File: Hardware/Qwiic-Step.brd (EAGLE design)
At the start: 50.8 x 50.8 mm, 99 parts, among them J1 PTH, J2 Qwiic Right Angle, J3 5.5x2.1mm Barrel, J4 Qwiic Right Angle, J5 ISP, U1 A4988ALT1, U2 ATMEGA328P_TQFP, Y1 16MHz

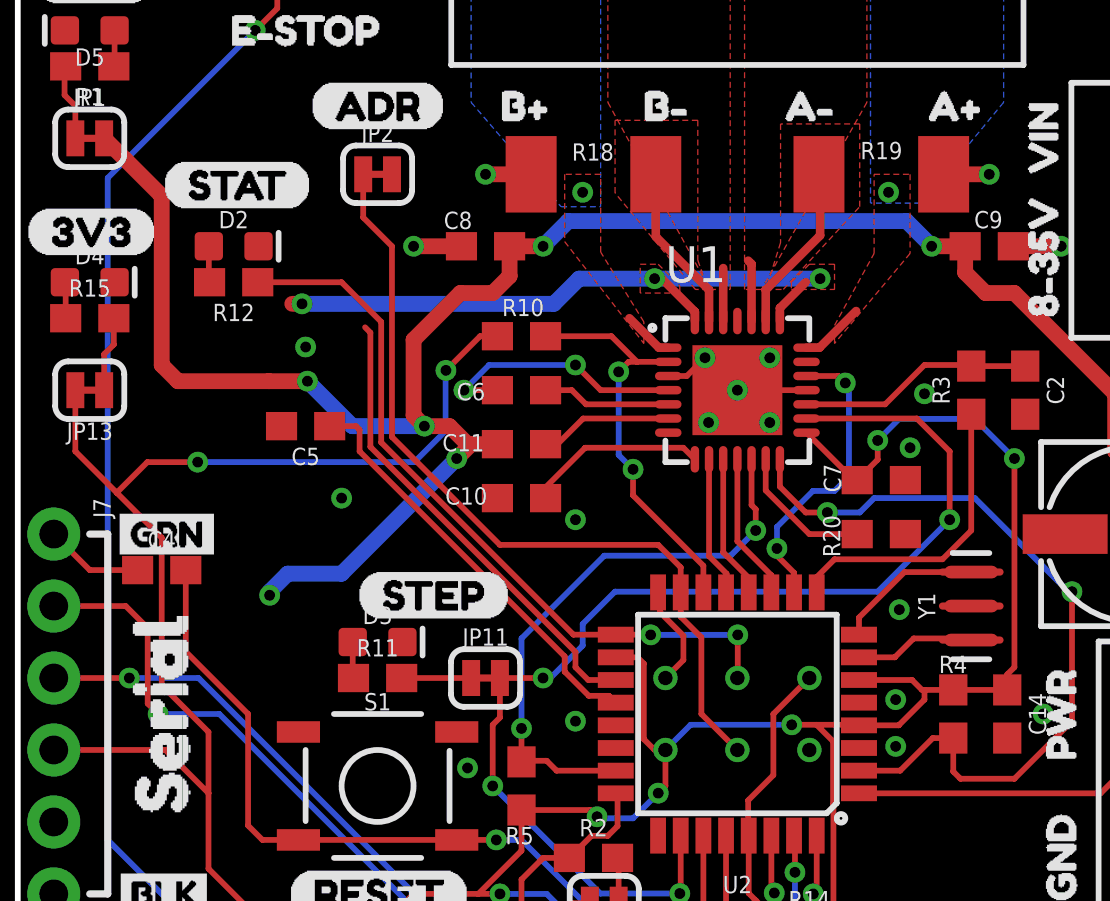
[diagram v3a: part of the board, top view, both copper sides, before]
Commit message: Cleaning up Rev 1 changes. Still need to connect current sense trace, run DRC.
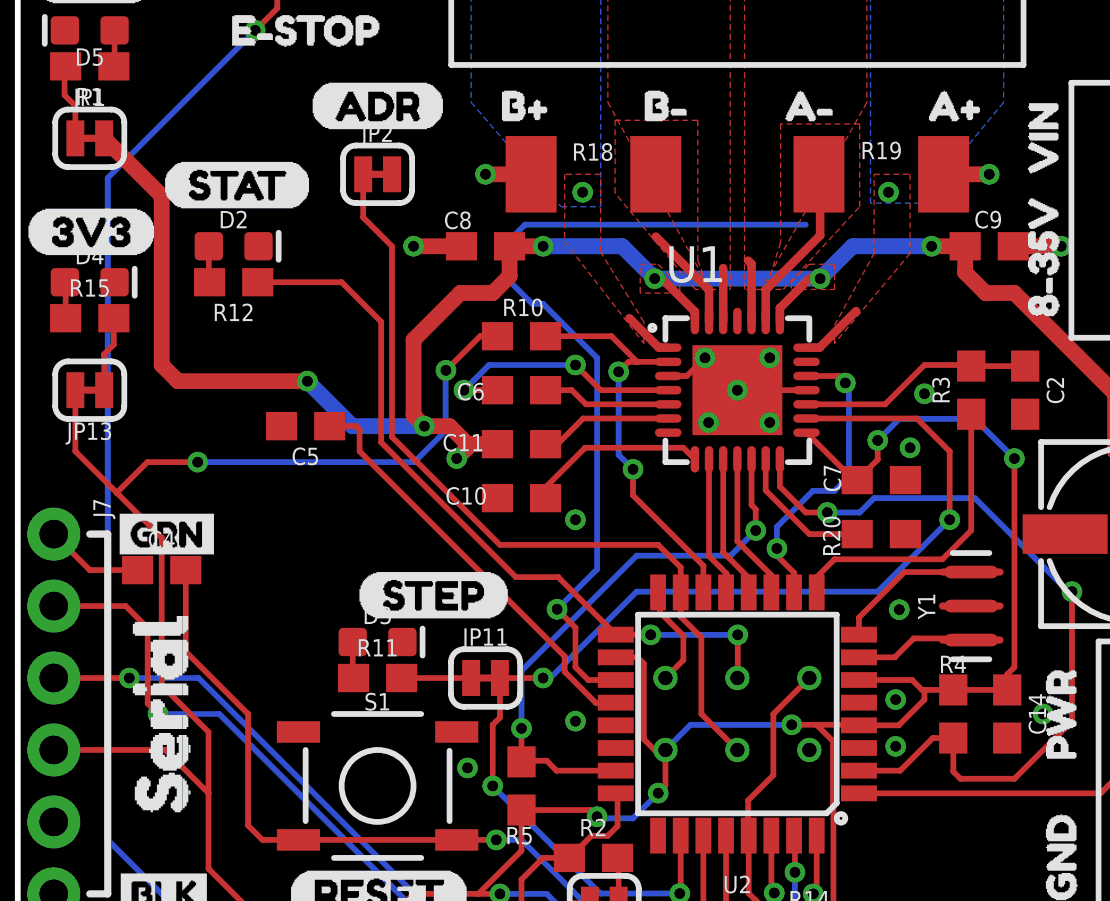
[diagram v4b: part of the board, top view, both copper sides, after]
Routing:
- net VIN: track 101.7 -> 74.8 mm, vias 9 -> 7
- net CURRENT_SENSE: track 22.7 -> 35.6 mm, vias 0 -> 1
- net N$31: track 5.96 -> 3.76 mm
- net A49885_!RESET!: track 20.2 -> 19.6 mm
- net GND: vias 22 -> 20

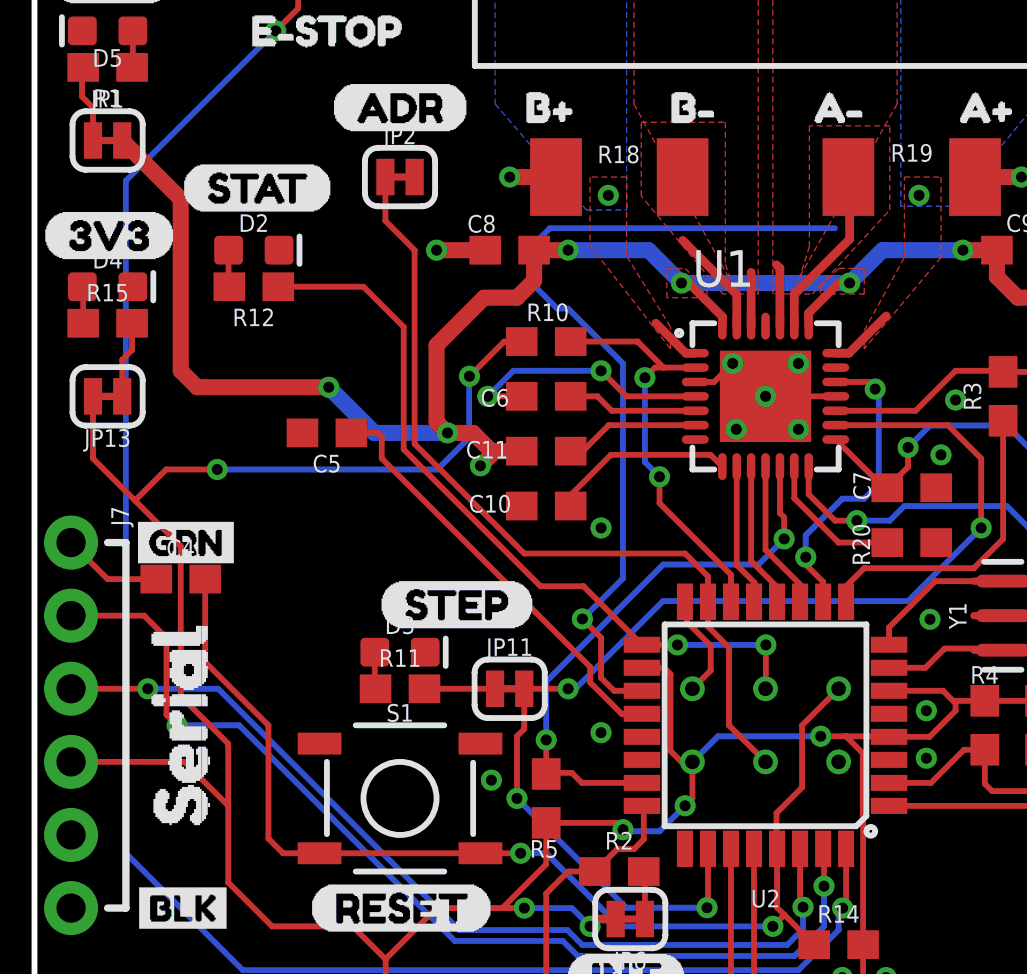
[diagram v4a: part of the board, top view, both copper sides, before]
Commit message: Added amplifier circuit to current sense reading
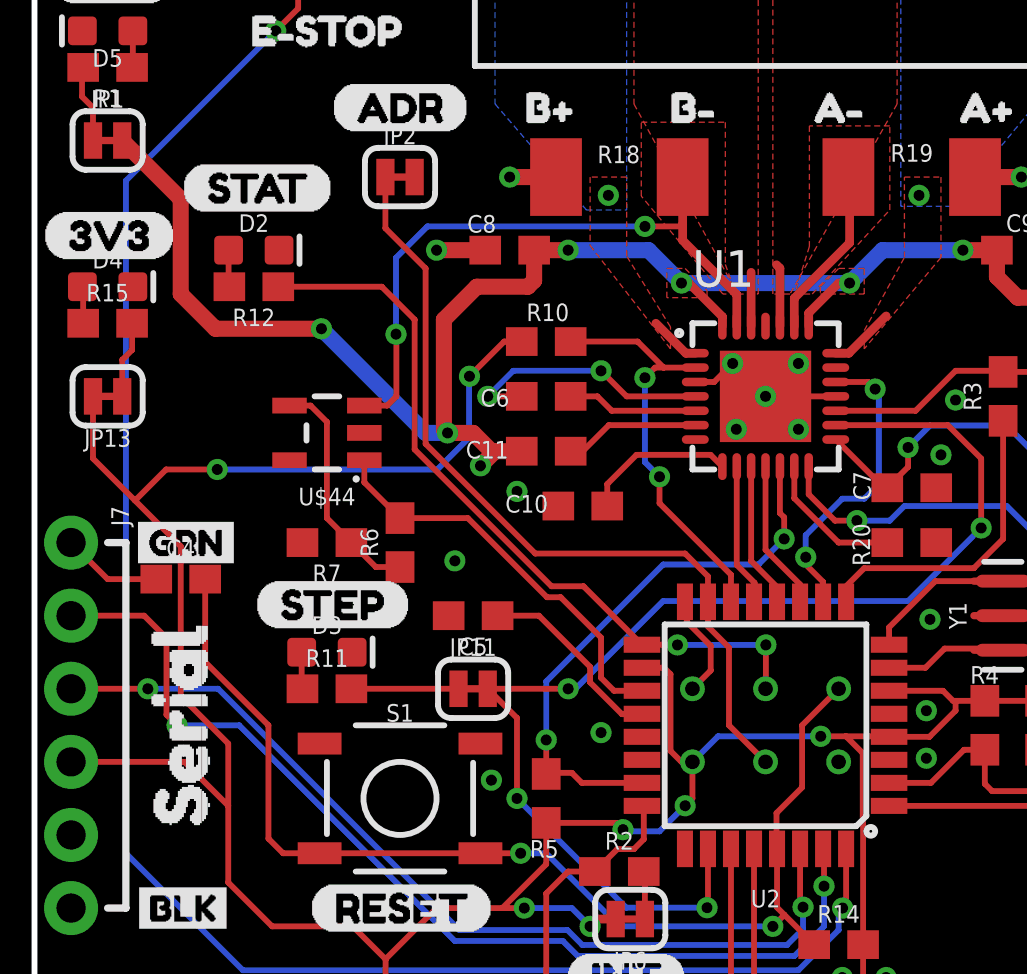
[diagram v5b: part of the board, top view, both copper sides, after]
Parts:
- added R6: 300k, SparkFun-Resistors:0603
- added R7: 1k, SparkFun-Resistors:0603
- added U$44: OPA344, SparkFun-IC-Amplifiers:SOT23-5
- moved C5 8.13 mm to (15.2, 19.1)
- moved U$32 7.62 mm to (36.8, 35.6)
- moved U$19 7.62 mm to (27.4, 31.5)
- moved LOGO1 7.49 mm to (20.2, 31.5)
- moved U$36 5.08 mm to (34.8, 41.8)
- moved U$37 5.08 mm to (29.7, 41.8)
- moved U$38 5.08 mm to (19.6, 41.8)
- moved U$39 5.08 mm to (24.5, 41.8)
- moved U$7 4.32 mm to (7.62, 19.4)
- moved D3 2.54 mm to (10.2, 17.8)
- moved R11 2.54 mm to (10.2, 16.5)
- moved JP11 1.27 mm to (15.2, 16.5)
- moved C10 1.27 mm to (19.1, 22.9)
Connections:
- removed net N$31: R18.2, U1.27
- new net AMP_CUR_SENSE: R6.2, U$44.1, U2.19
- new net N$2: R6.1, R7.1, U$44.4
- new net N$3: R19.2, U1.23
- net CURRENT_SENSE: now also R18.2, U$44.3, U1.27; no longer R19.2, U1.23, U2.19
- net GND: now also R7.2
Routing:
- net AMP_CUR_SENSE: track 0.00 -> 14.3 mm
- net CURRENT_SENSE: track 35.6 -> 22.5 mm, vias 1 -> 2
- net AREF: track 14.9 -> 6.76 mm
- net N$2: track 0.00 -> 8.12 mm
- net N$3: track 0.00 -> 5.99 mm
- net N$31: track 3.76 -> 0.00 mm
- net STEP: track 40.3 -> 41.9 mm
- net VIN: track 74.8 -> 73.4 mm
- net N$11: track 2.45 -> 3.72 mm
- net N$20: track 6.40 -> 5.35 mm
- net GND: vias 20 -> 21
- removed copper zone on layer 1, net N$31

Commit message: All traces routed, READY FOR BOARD REVIEW (other than some minor silk updates that I'll do tomorrow morning).
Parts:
- removed R6: 300k, SparkFun-Resistors:0603
- removed U$39: (no value), buzzard_labels (15):B#3
- added R9: 22k, SparkFun-Resistors:0603
- added U$45: (no value), buzzard_labels (28):3V31
- added U$46: (no value), buzzard_labels (28):A#3
- added U$47: (no value), buzzard_labels (28):A#4
- added U$48: (no value), buzzard_labels (28):B#5
- added U$49: (no value), buzzard_labels (28):B#6
- U$15: device buzzard_labels (15):A#0 -> buzzard_labels (28):A#3
- U$16: device buzzard_labels (15):A#1 -> buzzard_labels (28):A#4
- U$17: device buzzard_labels (15):B#2 -> buzzard_labels (28):B#5
- U$18: device buzzard_labels (15):B#3 -> buzzard_labels (28):B#6
- U$36: device buzzard_labels (15):A#0 -> buzzard_labels (28):PWR7
- U$37: device buzzard_labels (15):A#1 -> buzzard_labels (28):STEP2
- U$38: device buzzard_labels (15):B#2 -> buzzard_labels (28):VIN0
- moved U$36 29.9 mm to (41.9, 12.7), turned to 90 degrees
- moved U$37 23.7 mm to (8.89, 30.5)
- moved U$25 22.6 mm to (20.2, 16.4), flipped to the bottom
- moved JP2 20.9 mm to (17.8, 14.0), flipped to the bottom
- moved JP11 14.5 mm to (11.4, 30.5), flipped to the bottom
- moved R11 14.0 mm to (11.4, 30.5)
- moved U$7 13.3 mm to (0.25, 30.5)
- moved D3 13.0 mm to (7.62, 30.5), turned to 180 degrees
- moved JP13 12.6 mm to (11.4, 35.6), flipped to the bottom, turned to 0 degrees
- moved U$38 11.3 mm to (8.89, 38.1)
- moved R15 10.9 mm to (11.4, 35.6)
- moved R7 10.2 mm to (15.2, 30.5), turned to 90 degrees
- moved U$44 10.2 mm to (19.1, 30.5)
- moved JP1 9.25 mm to (11.4, 38.1), flipped to the bottom
- moved R1 8.89 mm to (11.4, 38.1), turned to 0 degrees
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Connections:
- new net N$6: JP2.1, U2.22
- net AMP_CUR_SENSE: now also R9.2; no longer R6.2
- net MOSI: no longer JP2.1
- net N$2: now also R9.1; no longer R6.1
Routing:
- net MOSI: track 28.8 -> 6.39 mm
- net STEP: track 41.9 -> 63.4 mm
- net CURRENT_SENSE: track 22.5 -> 8.49 mm, vias 2 -> 0
- net N$21: track 4.71 -> 14.3 mm
- net N$20: track 5.35 -> 13.2 mm
- net N$9: track 4.54 -> 11.0 mm
- net 3.3V: track 153.7 -> 147.3 mm
- net !ENABLE!: track 14.5 -> 20.2 mm
- net AMP_CUR_SENSE: track 14.3 -> 19.9 mm, vias 0 -> 2
- net COILB+: track 1.80 -> 6.92 mm, vias 1 -> 2
- net N$8: track 9.13 -> 12.9 mm, vias 2 -> 0
- net !RST!: track 39.6 -> 36.5 mm
- net DTR: track 3.49 -> 6.55 mm
- net N$2: track 8.12 -> 5.12 mm
- net N$6: track 0.00 -> 2.85 mm, vias 0 -> 1
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- removed copper zone on layer 1, net COILB+
